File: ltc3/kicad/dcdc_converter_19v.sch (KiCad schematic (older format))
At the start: 0 parts

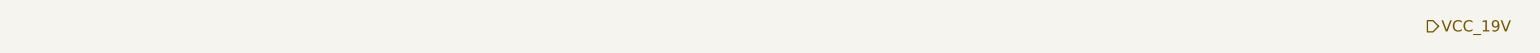
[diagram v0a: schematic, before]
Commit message: More work on LTC3 schematic. 1. Created placeholder "power in" schematic. 2. First cut at external trigger schematic (MOSTFETs and mechanical    relays).
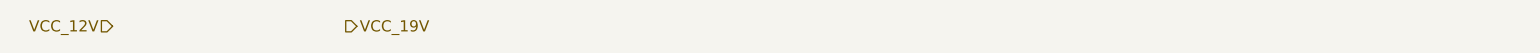
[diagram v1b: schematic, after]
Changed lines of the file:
@@
 LIBS:LTC299x
 LIBS:memory_devices
+LIBS:switches
 LIBS:Launch_Tower_Computer_III-cache
 EELAYER 27 0
@@
 $Descr USLetter 11000 8500
 encoding utf-8
-Sheet 4 4
+Sheet 4 6
 Title "LTC3 12V-to-19V DC/DC Converter"
-Date "16 mar 2015"
+Date "2 apr 2015"
 Rev "1"
 Comp "Portland State Aerospace Society <http://psas.pdx.edu/>"
@@
 Comment4 ""
 $EndDescr
-Text HLabel 9300 2150 2    60   Output ~ 0
+Text HLabel 3500 2150 2    60   Output ~ 0
 VCC_19V
+Text HLabel 2250 2150 0    60   Input ~ 0
+VCC_12V
 $EndSCHEMATC

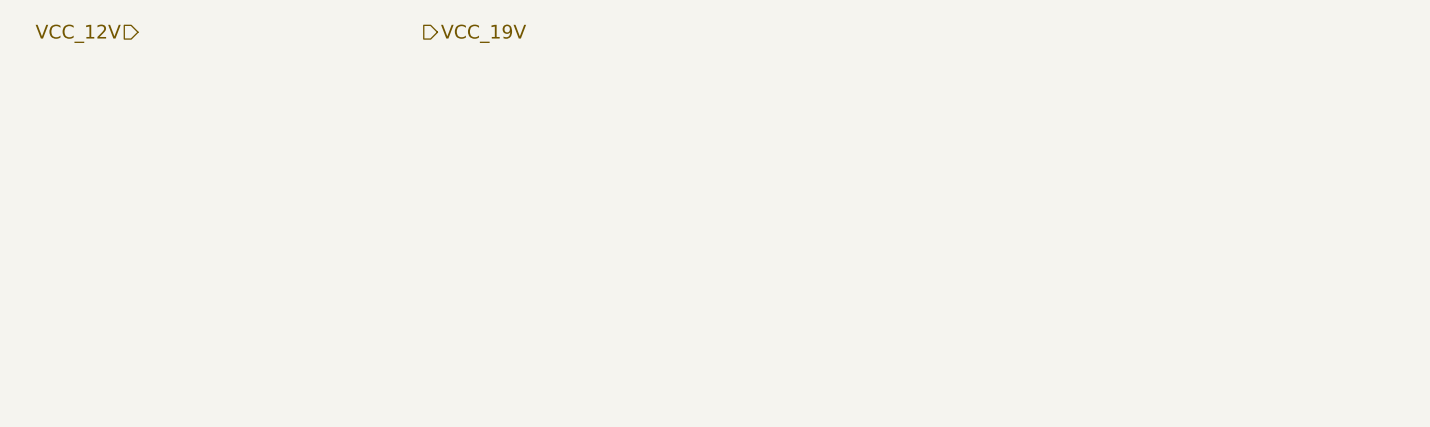
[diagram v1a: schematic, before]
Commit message: Fixed mistakes in triggers schematic; misc. clean-up.
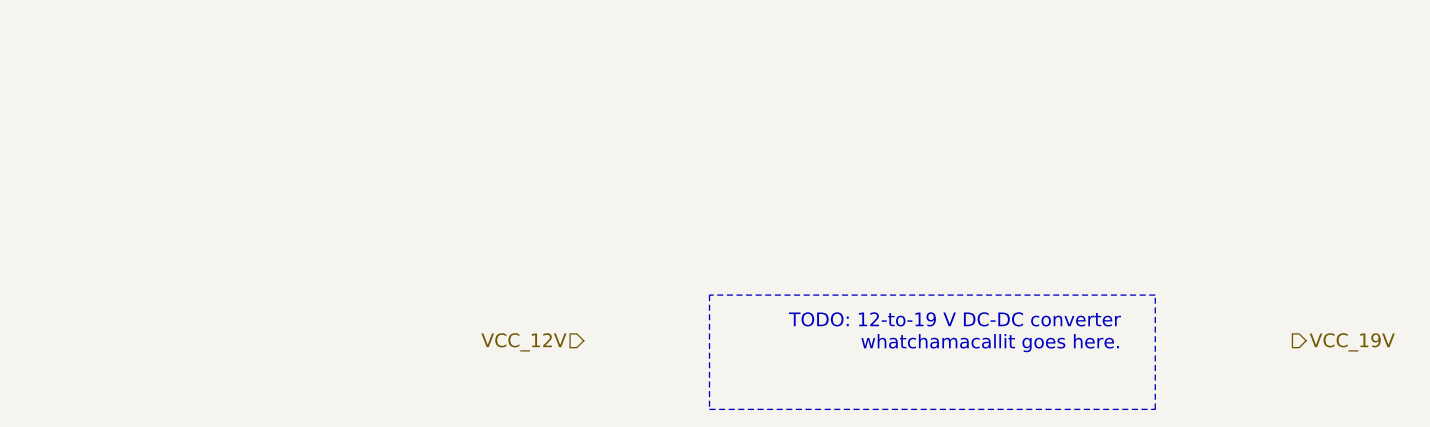
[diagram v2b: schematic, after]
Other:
- note added: "TODO: 12-to-19 V DC-DC converter\nwhatchamacallit goes here."
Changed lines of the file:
@@
 Comment4 ""
 $EndDescr
-Text HLabel 3500 2150 2    60   Output ~ 0
+Text HLabel 7300 3500 2    60   Output ~ 0
 VCC_19V
-Text HLabel 2250 2150 0    60   Input ~ 0
+Text HLabel 4200 3500 0    60   Input ~ 0
 VCC_12V
+Text Notes 6550 3550 2    60   ~ 0
+TODO: 12-to-19 V DC-DC converter\nwhatchamacallit goes here.
+Wire Notes Line
+	4750 3300 4750 3800
+Wire Notes Line
+	4750 3800 6700 3800
+Wire Notes Line
+	6700 3800 6700 3300
+Wire Notes Line
+	6700 3300 4750 3300
 $EndSCHEMATC

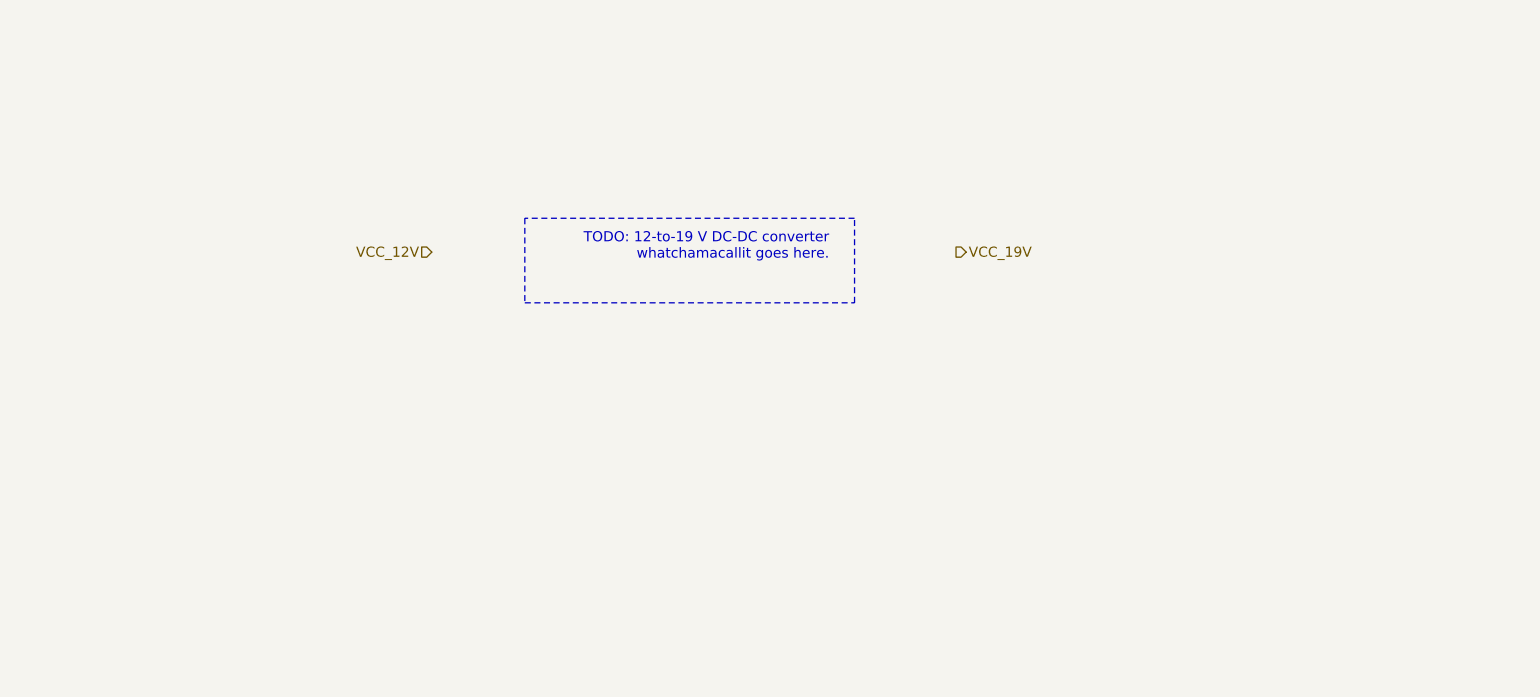
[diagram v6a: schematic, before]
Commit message: LTC3 KiCad updates. 1. Modified schematics to play nicely with (relatively) recent changes    in KiCad's stock component libraries (e.g., redrawn capacitor and    resistor symbols). 2. Began work on PTN78020-based DC-DC converter schematics.
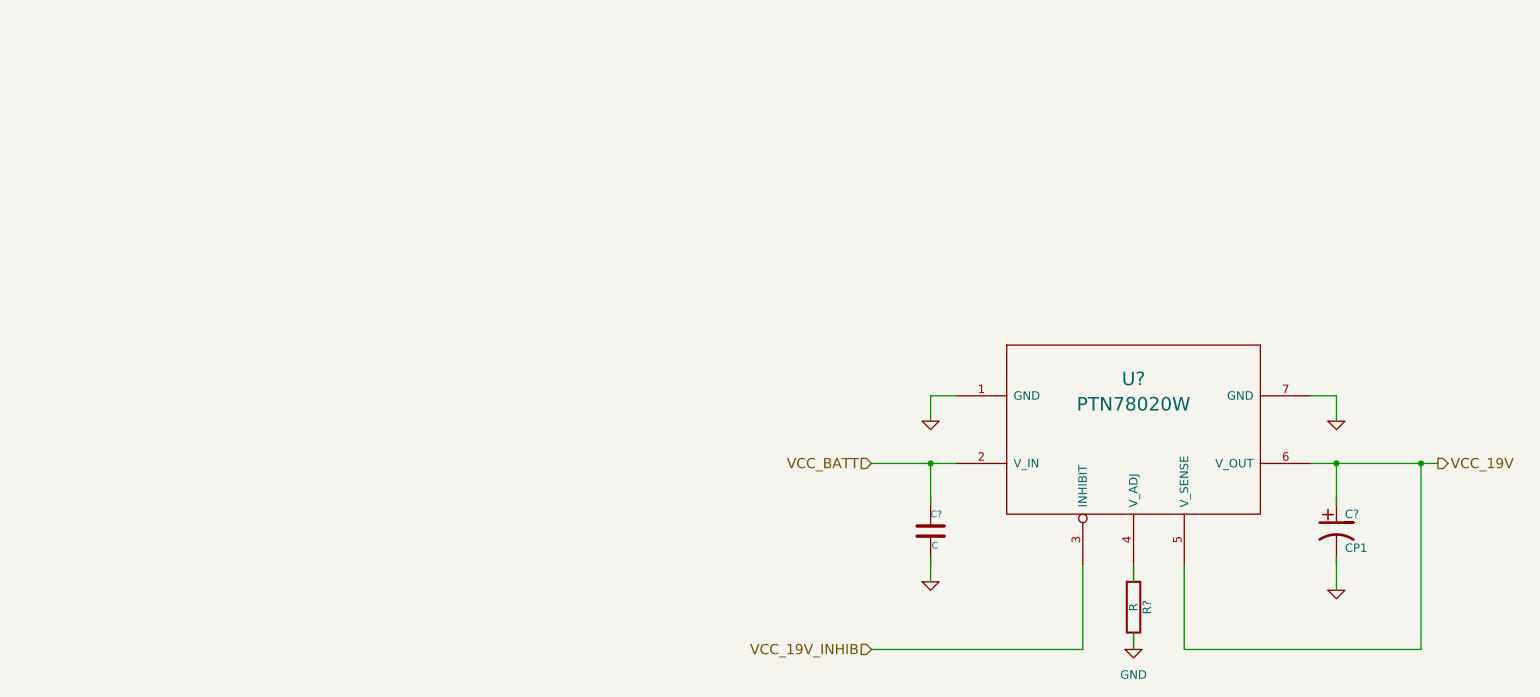
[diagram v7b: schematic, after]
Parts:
- added C?: CP1, ~, symbol CP1
- added C?: C, ~, symbol C
- added R?: R, symbol R
- added U?: PTN78020W, ~, symbol PTN78020W
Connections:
- net labels added: GND, VCC_19V_INHIB, VCC_BATT
- net labels removed: VCC_12V
- wire segments 0 -> 17
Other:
- note removed: "TODO: 12-to-19 V DC-DC converter\nwhatchamacallit goes here."
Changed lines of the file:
@@
 LIBS:memory
 LIBS:xilinx
-LIBS:special
 LIBS:microcontrollers
 LIBS:dsp
@@
 LIBS:switches
 LIBS:Toshiba
+LIBS:LTC3_components
 LIBS:Launch_Tower_Computer_III-cache
-EELAYER 27 0
+EELAYER 25 0
 EELAYER END
 $Descr B 17000 11000
@@
 Sheet 4 7
 Title "LTC3 12V-to-19V DC/DC Converter"
-Date "18 apr 2015"
+Date "16 may 2015"
 Rev "1"
 Comp "Portland State Aerospace Society <http://psas.pdx.edu/>"
@@
 Comment4 ""
 $EndDescr
-Text HLabel 7300 3500 2    60   Output ~ 0
+Text HLabel 10150 4750 2    60   Output ~ 0
 VCC_19V
-Text HLabel 4200 3500 0    60   Input ~ 0
-VCC_12V
-Text Notes 6550 3550 2    60   ~ 0
-TODO: 12-to-19 V DC-DC converter\nwhatchamacallit goes here.
-Wire Notes Line
-	4750 3300 4750 3800
-Wire Notes Line
-	4750 3800 6700 3800
-Wire Notes Line
-	6700 3800 6700 3300
-Wire Notes Line
-	6700 3300 4750 3300
+Text HLabel 6800 4750 0    60   Input ~ 0
+VCC_BATT
+$Comp
+L PTN78020W U?
+U 1 1 555D15B9
+P 8350 4550
+F 0 "U?" H 8350 4850 80  0000 C CNN
+F 1 "PTN78020W" H 8350 4700 80  0000 C CNN
+F 2 "~" H 8350 4600 60  0000 C CNN
+F 3 "~" H 8350 4600 60  0000 C CNN
+	1    8350 4550
+	1    0    0    -1
+$EndComp
+$Comp
+L GND #PWR?
+U 1 1 555D15C0
+P 7150 4500
+F 0 "#PWR?" H 7150 4500 30  0001 C CNN
+F 1 "GND" H 7150 4430 30  0001 C CNN
+F 2 "" H 7150 4500 60  0000 C CNN
+F 3 "" H 7150 4500 60  0000 C CNN
+	1    7150 4500
+	1    0    0    -1
+$EndComp
+$Comp
+L GND #PWR?
+U 1 1 555D15C6
+P 9550 4500
+F 0 "#PWR?" H 9550 4500 30  0001 C CNN
+F 1 "GND" H 9550 4430 30  0001 C CNN
+F 2 "" H 9550 4500 60  0000 C CNN
+F 3 "" H 9550 4500 60  0000 C CNN
+	1    9550 4500
+	1    0    0    -1
+$EndComp
+Wire Wire Line
+	7300 4350 7150 4350
+Wire Wire Line
+	7150 4350 7150 4500
+Wire Wire Line
+	9400 4350 9550 4350
+Wire Wire Line
+	9550 4350 9550 4500
+Wire Wire Line
+	9400 4750 10150 4750
+Wire Wire Line
+	6800 4750 7300 4750
+$Comp
+L CP1 C?
+U 1 1 555D15D2
+P 9550 5150
+F 0 "C?" H 9600 5250 50  0000 L CNN
+F 1 "CP1" H 9600 5050 50  0000 L CNN
+F 2 "~" H 9550 5150 60  0000 C CNN
+F 3 "~" H 9550 5150 60  0000 C CNN
+	1    9550 5150
+	1    0    0    -1
+$EndComp
+$Comp
+L GND #PWR?
+U 1 1 555D15D9
+P 9550 5500
+F 0 "#PWR?" H 9550 5500 30  0001 C CNN
+F 1 "GND" H 9550 5430 30  0001 C CNN
+F 2 "" H 9550 5500 60  0000 C CNN
+F 3 "" H 9550 5500 60  0000 C CNN
+	1    9550 5500
+	1    0    0    -1
+$EndComp
+Wire Wire Line
+	9550 5000 9550 4750
+Connection ~ 9550 4750
+Wire Wire Line
+	9550 5300 9550 5500
+$Comp
+L C C?
+U 1 1 555D15E2
+P 7150 5150
+F 0 "C?" H 7150 5250 40  0000 L CNN
+F 1 "C" H 7156 5065 40  0000 L CNN
+F 2 "~" H 7188 5000 30  0000 C CNN
+F 3 "~" H 7150 5150 60  0000 C CNN
+	1    7150 5150
+	1    0    0    -1
+$EndComp
+$Comp
+L GND #PWR?
+U 1 1 555D15E9
+P 7150 5450
+F 0 "#PWR?" H 7150 5450 30  0001 C CNN
+F 1 "GND" H 7150 5380 30  0001 C CNN
+F 2 "" H 7150 5450 60  0000 C CNN
+F 3 "" H 7150 5450 60  0000 C CNN
+	1    7150 5450
+	1    0    0    -1
+$EndComp
+Wire Wire Line
+	7150 5450 7150 5300
+Wire Wire Line
+	7150 5000 7150 4750
+Connection ~ 7150 4750
+$Comp
+L R R?
+U 1 1 555D15F2
+P 8350 5600
+F 0 "R?" V 8430 5600 50  0000 C CNN
+F 1 "R" V 8350 5600 50  0000 C CNN
+F 2 "" V 8280 5600 30  0000 C CNN
+F 3 "" H 8350 5600 30  0000 C CNN
+	1    8350 5600
+	1    0    0    -1
+$EndComp
+$Comp
+L GND #PWR?
+U 1 1 555D15F9
+P 8350 5850
+F 0 "#PWR?" H 8350 5600 50  0001 C CNN
+F 1 "GND" H 8350 5700 50  0000 C CNN
+F 2 "" H 8350 5850 60  0000 C CNN
+F 3 "" H 8350 5850 60  0000 C CNN
+	1    8350 5850
+	1    0    0    -1
+$EndComp
+Wire Wire Line
+	8350 5850 8350 5750
+Wire Wire Line
+	8350 5450 8350 5350
+Text HLabel 6800 5850 0    60   Input ~ 0
+VCC_19V_INHIB
+Wire Wire Line
+	8050 5350 8050 5850
+Wire Wire Line
+	8050 5850 6800 5850
+Wire Wire Line
+	8650 5350 8650 5850
+Wire Wire Line
+	8650 5850 10050 5850
+Wire Wire Line
+	10050 5850 10050 4750
+Connection ~ 10050 4750
 $EndSCHEMATC
